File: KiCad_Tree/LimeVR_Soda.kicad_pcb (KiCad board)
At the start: 2 copper layers, 29.2 x 26.2 mm, 15 parts, among them J1 Power_IN, J2 Extension_Module, J3 UART, J4 GND, J5 CHIP_PU, J6 Power_OUT, J7 IMU_Pin_Header, U1 ESP8684-WROOM-02C

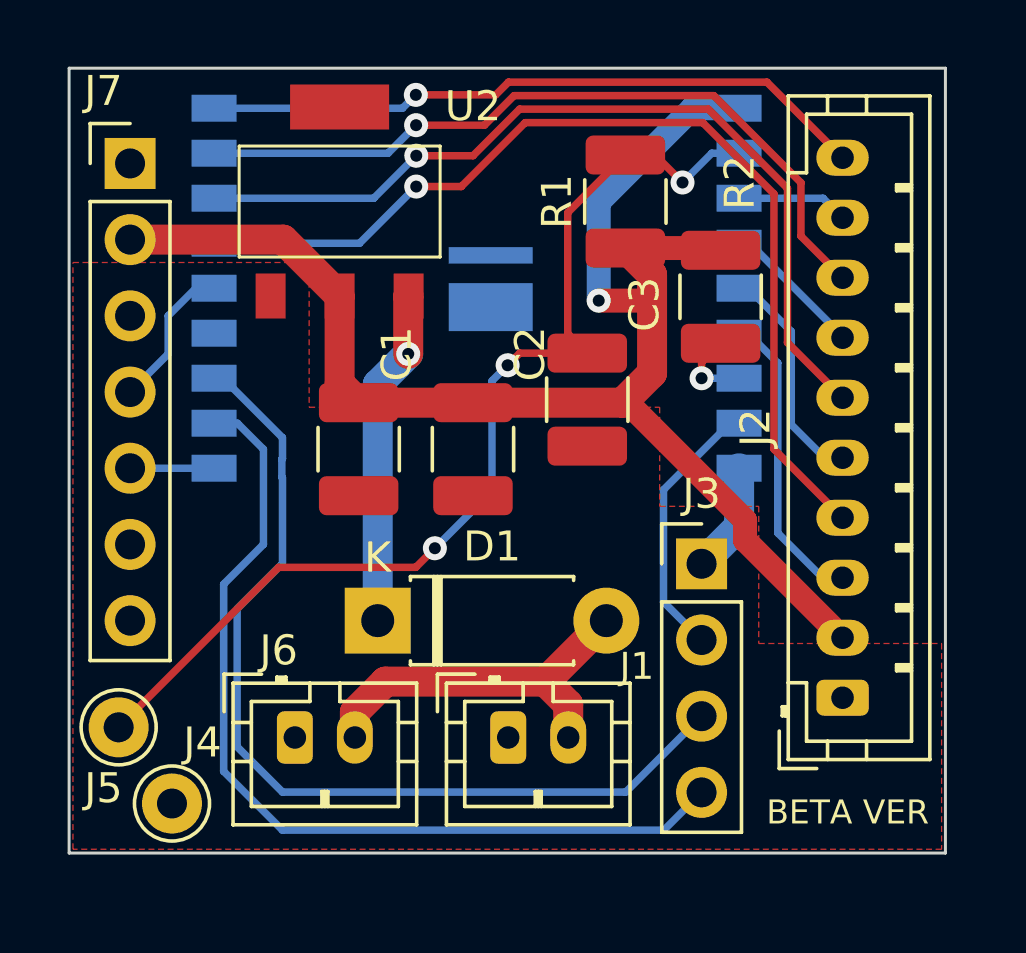
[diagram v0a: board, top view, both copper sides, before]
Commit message: v1.2 一个无聊又可悲的版本
我恨 esp-idf
总之，等 platformIO 支持 esp32-c2 了或许可以装上官方的固件吧
那样这些时间也不算是完全浪费
又或许 c2 和 c3 的引脚什么的都是兼容的，倒是能基本直接换掉
无聊
但也没那么无聊吧，至少让我找到了不少事情干，espidf
的文档要是写的更详细点，或许我现在也不会失去动力了吧
谁能想到所有技术栈里 freertos 和抄来的 kalmanFilter 都能弄好
最后被一个 i2c 和 spi 的驱动教训呢

这些东西感觉出现在 readme 里会更好
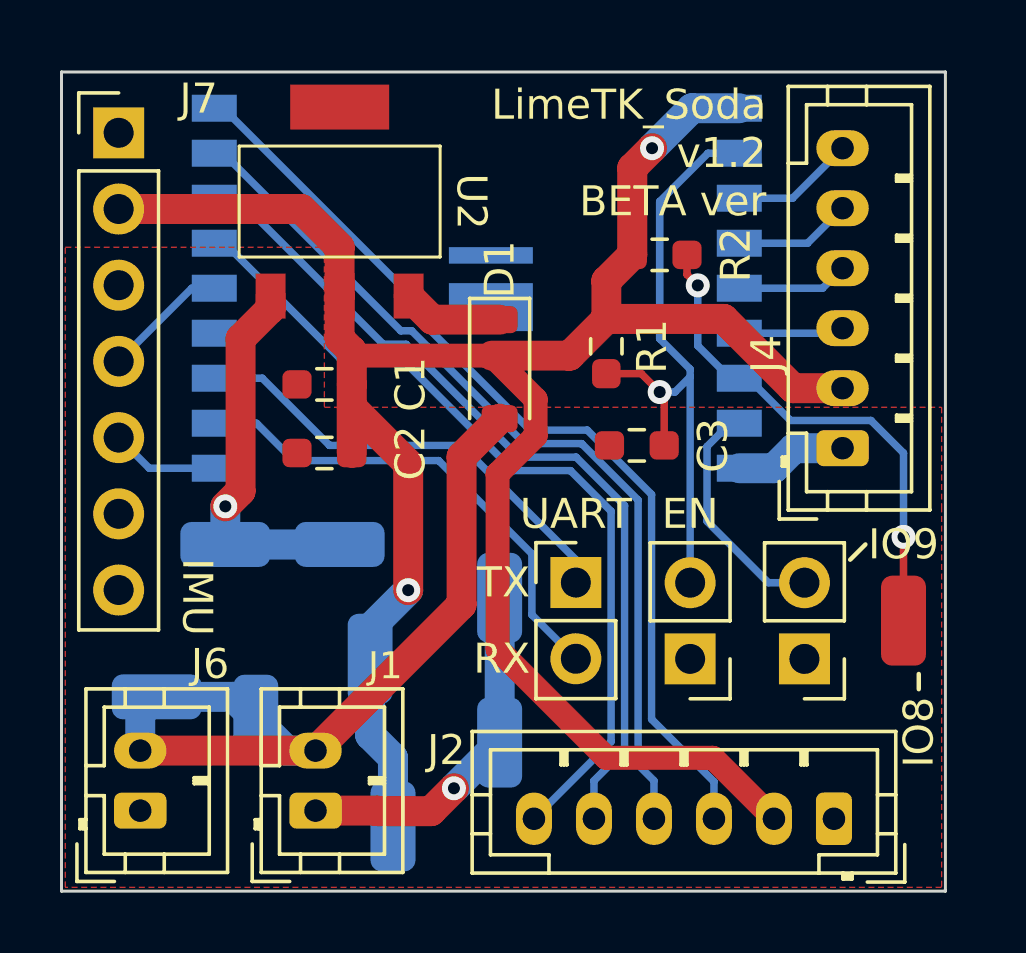
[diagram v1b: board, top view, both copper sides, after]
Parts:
- added J10: GND Pad, SourLemonJuice:Wire_Pad_1.5x3, B.Cu at (131.1, 103.4)
- added J11: GND Pad, SourLemonJuice:Wire_Pad_1.5x3, B.Cu at (131.1, 108.2)
- added J12: V3.3 Pad, SourLemonJuice:Wire_Pad_1.5x3, B.Cu at (126.7, 105.4)
- added J13: V3.3 Pad, SourLemonJuice:Wire_Pad_1.5x3, B.Cu at (127.5, 111.0)
- added J14: GND Pad, SourLemonJuice:Wire_Pad_1.5x3, B.Cu at (121.9, 101.6)
- added J15: V5 Pad, SourLemonJuice:Wire_Pad_1.5x3, B.Cu at (119.6, 106.7)
- added J16: GND Pad, SourLemonJuice:Wire_Pad_1.5x3, B.Cu at (125.7, 101.6)
- added J17: V5 Pad, SourLemonJuice:Wire_Pad_1.5x3, B.Cu at (122.9, 107.4)
- added J8: CHIP_PU_Pinheader, Connector_PinHeader_2.54mm:PinHeader_1x02_P2.54mm_Vertical, F.Cu at (137.4, 105.4)
- added J9: GPIO9_Pinheader, Connector_PinHeader_2.54mm:PinHeader_1x02_P2.54mm_Vertical, F.Cu at (141.2, 105.4)
- C1, C2, C3, R1, R2: footprint Resistor_SMD:R_1210_3225Metric_Pad1.30x2.65mm_HandSolder -> Resistor_SMD:R_0603_1608Metric_Pad0.98x0.95mm_HandSolder
- D1: value 1N5817 -> 1N5817W; footprint Diode_THT:D_DO-41_SOD81_P7.62mm_Horizontal -> Diode_SMD:D_SOD-123
- J1: value Power_IN -> JST_PH-2p
- J2: value Extension_Module -> Extension_Module_1_PH-6p; footprint Connector_JST:JST_PH_B10B-PH-K_1x10_P2.00mm_Vertical -> Connector_JST:JST_PH_B6B-PH-K_1x06_P2.00mm_Vertical
- J3: value UART -> UART_Pinheader; footprint Connector_PinHeader_2.54mm:PinHeader_1x04_P2.54mm_Vertical -> Connector_PinHeader_2.54mm:PinHeader_1x02_P2.54mm_Vertical
- J4: value GND -> Extension_Module_2_PH-6p; footprint Connector_Pin:Pin_D1.0mm_L10.0mm -> Connector_JST:JST_PH_B6B-PH-K_1x06_P2.00mm_Vertical
- J5: value CHIP_PU -> Extension_3_pad; footprint Connector_Pin:Pin_D1.0mm_L10.0mm -> SourLemonJuice:Wire_Pad_1.5x3
- J6: value Power_OUT -> JST_PH-2p
- J7: value IMU_Pin_Header -> IMU_BMI160_Module
- moved J5 26.4 mm to (144.5, 104.1), turned to 90 degrees
- moved J4 25.3 mm to (142.5, 98.4), turned to 90 degrees
- moved D1 9.32 mm to (131.1, 95.8), turned to -90 degrees
- moved J1 6.87 mm to (124.9, 110.5), turned to 90 degrees
- moved J6 5.70 mm to (119.1, 110.5), turned to 90 degrees
- moved C2 4.95 mm to (125.2, 98.6), turned to 180 degrees
- moved R1 4.87 mm to (134.6, 95.0), turned to -90 degrees
- moved J3 4.24 mm to (133.6, 102.9)
- moved J2 4.04 mm to (142.2, 110.7), turned to 180 degrees
- moved R2 2.47 mm to (136.4, 91.9), turned to 0 degrees
- moved C1 2.44 mm to (125.2, 96.3), turned to 180 degrees
- moved C3 2.25 mm to (135.6, 98.3), turned to 180 degrees
- moved J7 1.09 mm to (118.4, 87.9)
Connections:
- J3 pad 1: GND -> /U0TXD
- J3 pad 2: /GIPO9 -> /U0RXD
- J5 pad 1: /Chip_PU -> Net-(J5-Pin_1)
- R2 pad 2: Net-(U1-GPIO8) -> Net-(J5-Pin_1)
- U1 pad 15: Net-(J2-Pin_4) -> Net-(J2-Pin_6)
- U1 pad 16: Net-(J2-Pin_6) -> Net-(J2-Pin_5)
- U1 pad 17: Net-(J2-Pin_8) -> Net-(J2-Pin_4)
- U1 pad 18: Net-(J2-Pin_10) -> Net-(J2-Pin_3)
- U1 pad 3: Net-(J2-Pin_9) -> Net-(J4-Pin_6)
- U1 pad 4: Net-(J2-Pin_7) -> Net-(J4-Pin_5)
- U1 pad 5: Net-(J2-Pin_5) -> Net-(J4-Pin_4)
- U1 pad 6: Net-(J2-Pin_3) -> Net-(J4-Pin_3)
- U1 pad 7: Net-(U1-GPIO8) -> Net-(J5-Pin_1)
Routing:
- net /VCC_3v3: track 51.6 -> 80.6 mm, vias 1 -> 2
- net Net-(J2-Pin_8): track 25.3 -> 0.00 mm, vias 1 -> 0
- net GND: track 3.71 -> 28.7 mm, vias 0 -> 2
- net Net-(J2-Pin_10): track 22.4 -> 0.00 mm, vias 1 -> 0
- net Net-(J2-Pin_3): track 10.1 -> 31.9 mm
- net Net-(J2-Pin_5): track 7.98 -> 28.8 mm
- net Net-(J5-Pin_1): track 0.00 -> 17.1 mm, vias 0 -> 2
- net /U0TXD: track 31.2 -> 15.3 mm
- net Net-(D1-A): track 12.7 -> 27.5 mm
- net /Chip_PU: track 36.2 -> 21.5 mm, vias 3 -> 1
- net /U0RXD: track 30.6 -> 16.5 mm
- net Net-(D1-K): track 11.2 -> 3.36 mm, vias 1 -> 0
- net Net-(J2-Pin_7): track 4.78 -> 0.00 mm
- net Net-(J4-Pin_6): track 0.00 -> 4.13 mm
- net Net-(J2-Pin_4): track 33.7 -> 29.8 mm, vias 1 -> 0
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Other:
- board size 29.2 x 26.2 mm -> 29.5 x 27.3 mm
- board text added: "3v3"
- board text added: "Extension 1"
- board text added: "Extension 2"
- board text added: "G"
- board text added: "GND"
- board text added: "LimeTK_Soda v1.2 BETA ver"
- board text added: "Power_IN"
- board text added: "V"
- board text added: "v5"
- board text removed: "5V_IN"
- board text removed: "5V_OUT"
- board text removed: "BETA VER"
- board text removed: "EN"
- board text removed: "Extension Module"
